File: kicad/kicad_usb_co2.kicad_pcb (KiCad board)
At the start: 2 copper layers, 72 x 47 mm, 9 parts, among them SW1 SW_SPDT, SW2 SW_SPDT, U1 MH-Z19B, U2 SeeeduinoXIAO, U3 MH-Z14A, U4 PinHeader_XIAO, U5 PinHeader_XIAO

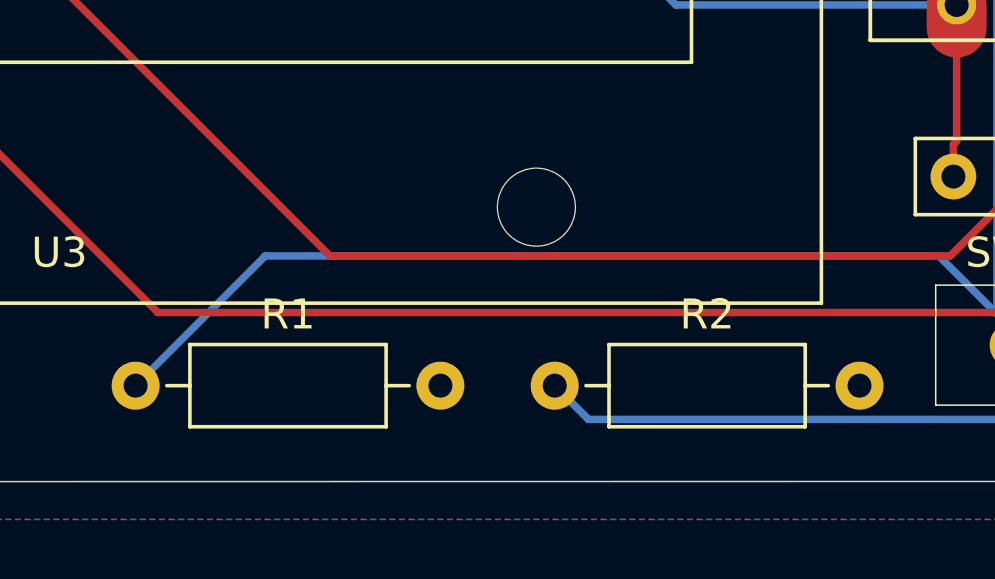
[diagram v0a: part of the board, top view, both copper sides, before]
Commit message: 抵抗の容量をシルクで書いた
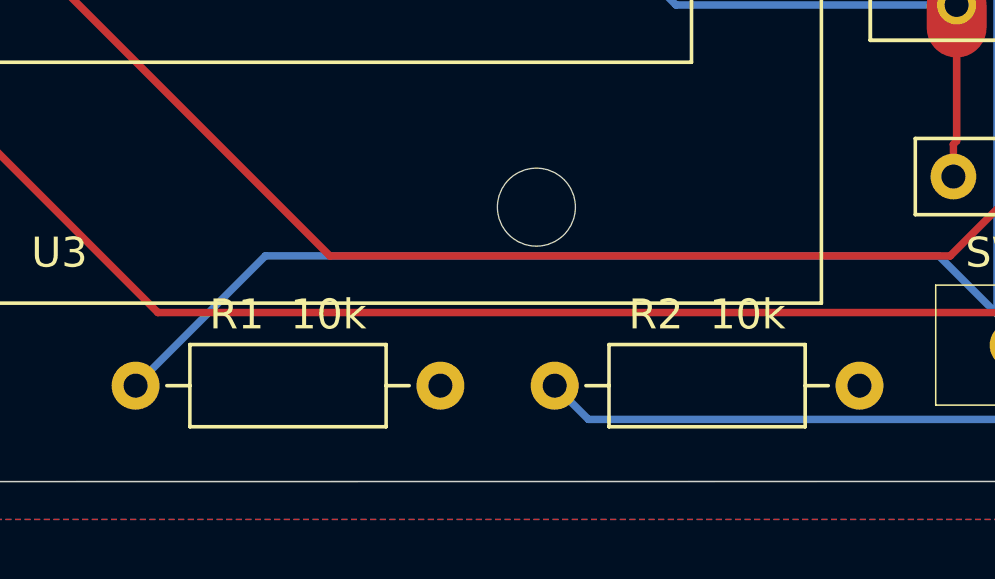
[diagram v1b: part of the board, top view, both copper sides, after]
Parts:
- R1  10k: renamed from R1
- R2  10k: renamed from R2
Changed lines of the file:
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@@
     (descr "Resistor, Axial_DIN0207 series, Axial, Horizontal, pin pitch=10.16mm, 0.25W = 1/4W, length*diameter=6.3*2.5mm^2, http://cdn-reichelt.de/documents/datenblatt/B400/1_4W%23YAG.pdf")
     (tags "Resistor Axial_DIN0207 series Axial Horizontal pin pitch 10.16mm 0.25W = 1/4W length 6.3mm diameter 2.5mm")
-    (fp_text reference R1 (at 5.08 -2.37) (layer F.SilkS)
+    (fp_text reference "R1  10k" (at 5.08 -2.37) (layer F.SilkS)
       (effects (font (size 1 1) (thickness 0.15)))
     )
@@
     (descr "Resistor, Axial_DIN0207 series, Axial, Horizontal, pin pitch=10.16mm, 0.25W = 1/4W, length*diameter=6.3*2.5mm^2, http://cdn-reichelt.de/documents/datenblatt/B400/1_4W%23YAG.pdf")
     (tags "Resistor Axial_DIN0207 series Axial Horizontal pin pitch 10.16mm 0.25W = 1/4W length 6.3mm diameter 2.5mm")
-    (fp_text reference R2 (at 5.08 -2.37) (layer F.SilkS)
+    (fp_text reference "R2  10k" (at 5.08 -2.37) (layer F.SilkS)
       (effects (font (size 1 1) (thickness 0.15)))
     )

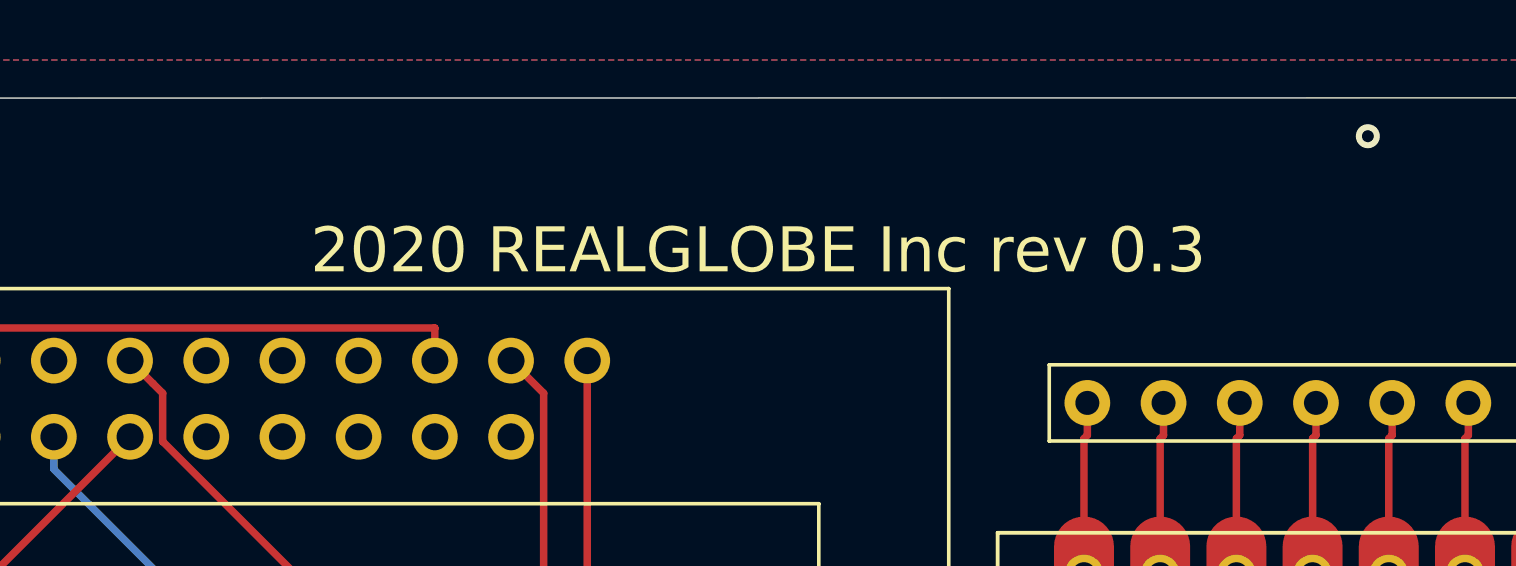
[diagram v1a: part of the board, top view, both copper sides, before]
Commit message: 基板リビジョンシルクをインクリメントした
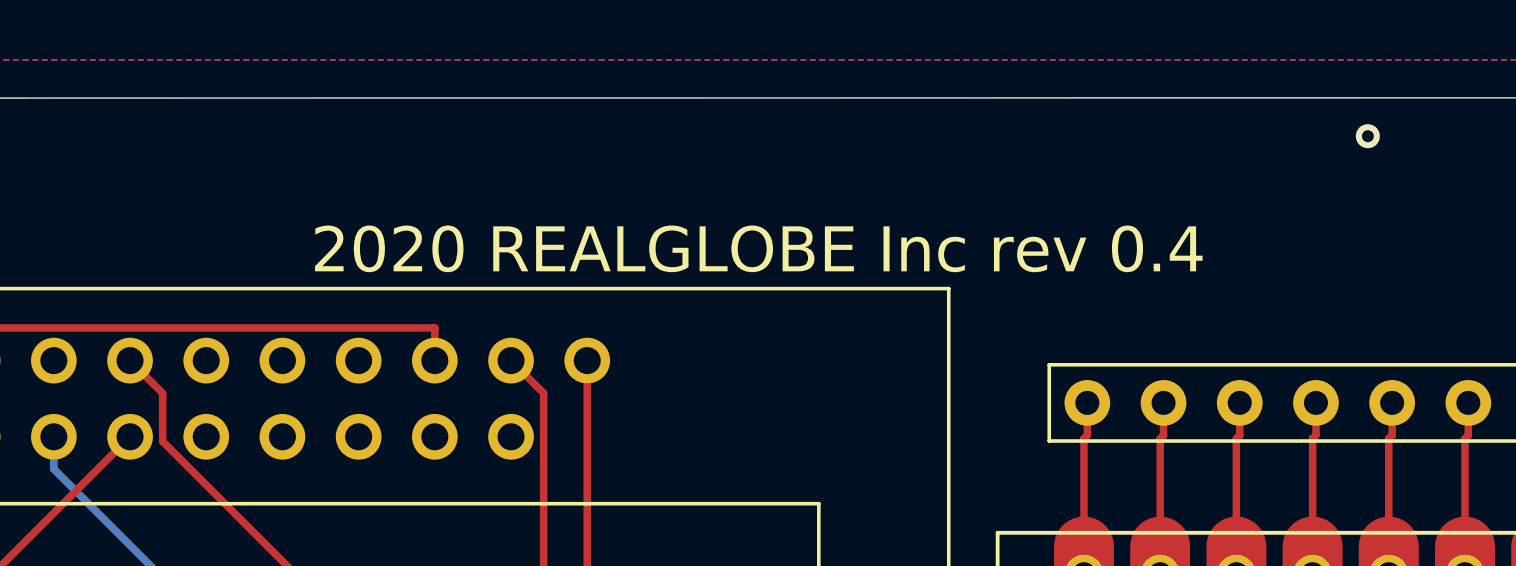
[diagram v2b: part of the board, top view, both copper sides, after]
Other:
- board text added: "2020 REALGLOBE Inc rev 0.4"
- board text removed: "2020 REALGLOBE Inc rev 0.3"
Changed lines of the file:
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@@
   (gr_circle (center 3 -44) (end 4.6 -44) (layer Edge.Cuts) (width 0.05))
   (gr_arc (start 2.54 -44.45) (end 2.54 -46.99) (angle -90) (layer Edge.Cuts) (width 0.05))
-  (gr_text "2020 REALGLOBE Inc rev 0.3" (at 33.02 -41.91) (layer F.SilkS)
+  (gr_text "2020 REALGLOBE Inc rev 0.4\n" (at 33.02 -41.91) (layer F.SilkS)
     (effects (font (size 1.5 1.5) (thickness 0.3)))
   )

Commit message: 署名を変更
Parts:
- added ~: signature_koino, kicad_mylib:signature_koino, F.Cu at (6.35, -41.9)
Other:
- board text removed: "2020 REALGLOBE Inc rev 0.4"
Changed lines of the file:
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@@
   (general
     (thickness 1.6)
-    (drawings 17)
+    (drawings 16)
     (tracks 104)
     (zones 0)
-    (modules 9)
+    (modules 10)
     (nets 34)
   )
@@
     (add_net "Net-(U3-Pad7)")
     (add_net "Net-(U3-Pad9)")
+  )
+  (module kicad_mylib:signature_koino (layer F.Cu)
+    (at 6.35 -41.91)
+    (fp_text reference ~ (at 2.54 -3.81) (layer F.SilkS)
+      (effects (font (size 1 1) (thickness 0.15)))
+    )
+    (fp_text value signature_koino (at 6.35 -5.58) (layer F.Fab)
+      (effects (font (size 1 1) (thickness 0.15)))
+    )
+    (fp_text user "Twitter:@koino_mfg  USB-co2" (at 0 -1.27) (layer F.SilkS)
+      (effects (font (size 1 1) (thickness 0.15)) (justify left))
+    )
   )
   (module kicad_mylib:MH-Z19B (layer F.Cu)
@@
   (gr_circle (center 3 -44) (end 4.6 -44) (layer Edge.Cuts) (width 0.05))
   (gr_arc (start 2.54 -44.45) (end 2.54 -46.99) (angle -90) (layer Edge.Cuts) (width 0.05))
-  (gr_text "2020 REALGLOBE Inc rev 0.4\n" (at 33.02 -41.91) (layer F.SilkS)
-    (effects (font (size 1.5 1.5) (thickness 0.3)))
-  )
   (gr_circle (center 3 -3) (end 4.6 -3) (layer Edge.Cuts) (width 0.05))
   (gr_circle (center 69 -44) (end 70.6 -44) (layer Edge.Cuts) (width 0.05))
